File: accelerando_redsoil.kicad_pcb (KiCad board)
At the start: 2 copper layers, 24.1 x 26.7 mm, 8 parts, among them J1 Conn_01x10, J2 Conn_01x10, J3 Conn_01x05_Female, J4 Conn_01x04_Male, U1 eByte E73-2G4M08S1C-52840

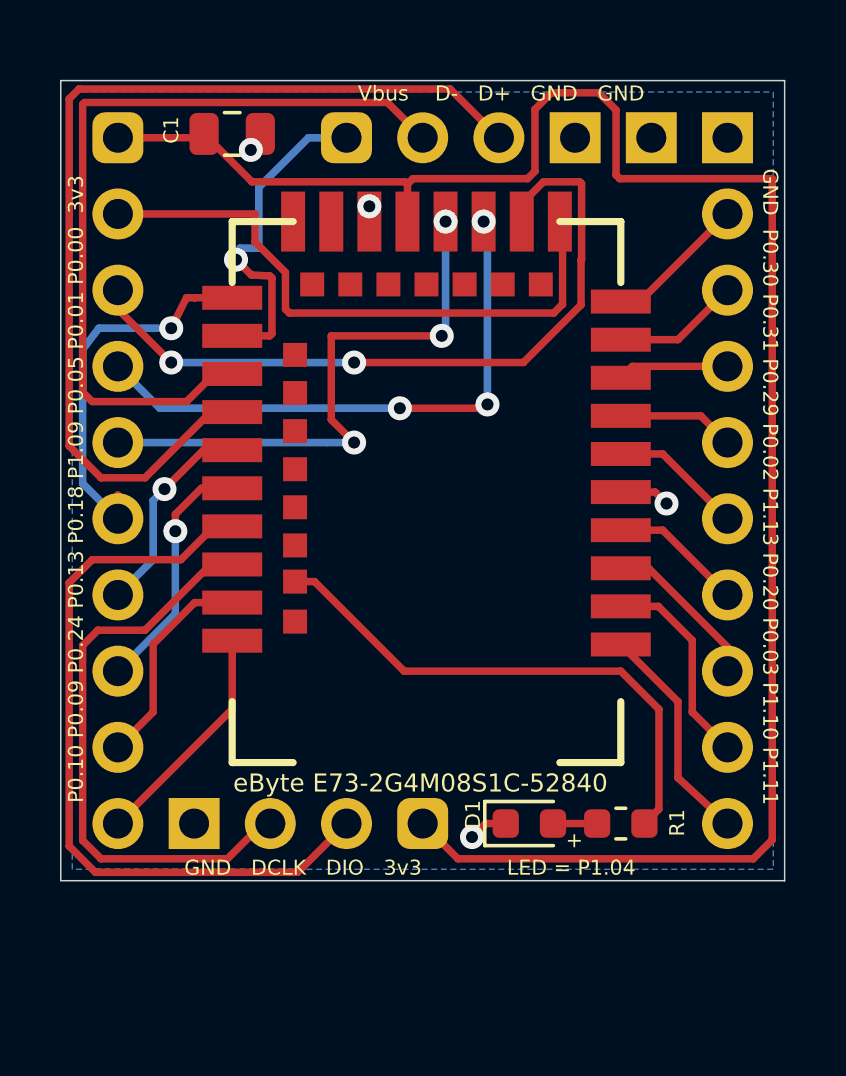
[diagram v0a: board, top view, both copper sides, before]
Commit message: Redsoil PCB 1.1 - USB power, Battery conn, JST PH SWD
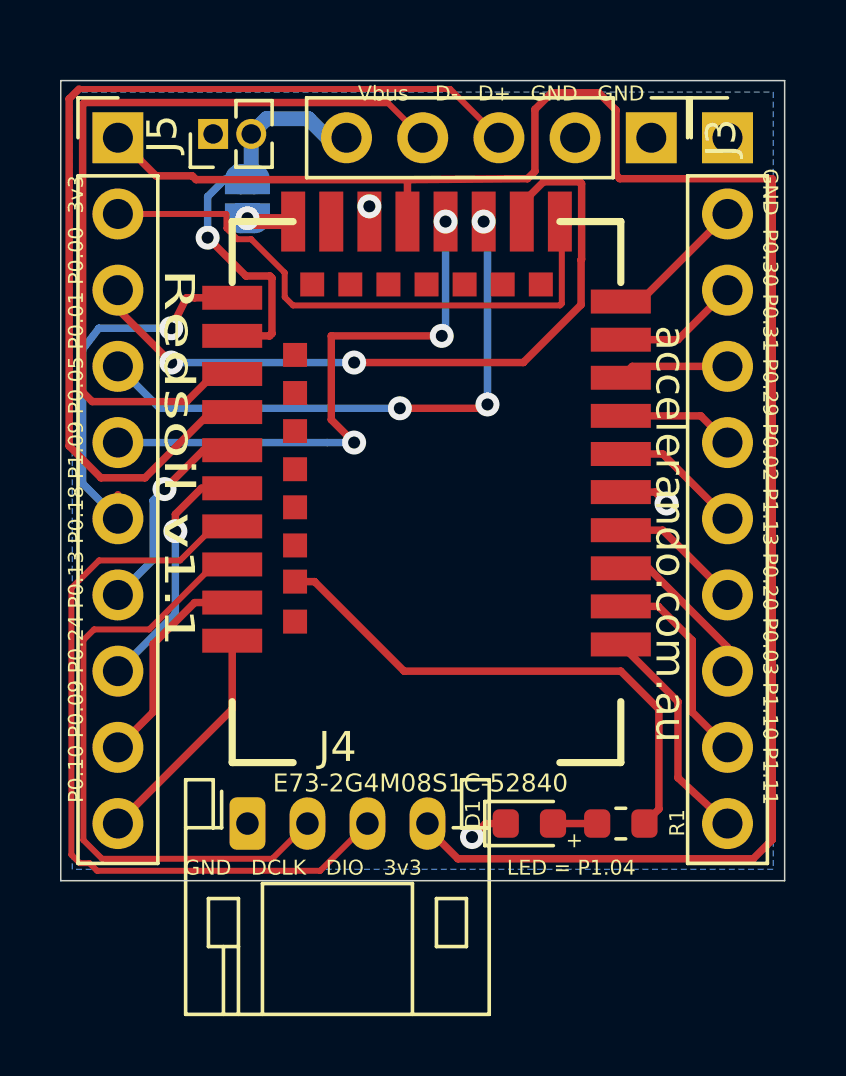
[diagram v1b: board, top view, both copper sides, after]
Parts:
- removed C1: C, Capacitor_SMD:C_0805_2012Metric
- added J5: Batt, Connector_PinHeader_1.27mm:PinHeader_1x02_P1.27mm_Vertical, F.Cu at (92.1, 58.3)
- added JP1: Jumper_2_Bridged, Jumper:SolderJumper-2_P1.3mm_Open_RoundedPad1.0x1.5mm, B.Cu at (93.2, 60.5)
- J1: value Conn_01x10 -> IOA; footprint Accelerando:PinHeader_1x10_P2.54mm_Vertical_nooutline -> Connector_PinHeader_2.54mm:PinHeader_1x10_P2.54mm_Vertical
- J2: value Conn_01x10 -> IOB; footprint Accelerando:PinHeader_1x10_P2.54mm_Vertical_nooutline -> Connector_PinHeader_2.54mm:PinHeader_1x10_P2.54mm_Vertical
- J3: value Conn_01x05_Female -> USB; footprint Accelerando:PinHeader_1x05_P2.54mm_Vertical_nooutline -> Connector_PinHeader_2.54mm:PinHeader_1x05_P2.54mm_Vertical
- J4: value Conn_01x04_Male -> SWD; footprint Connector_PinHeader_2.54mm:PinHeader_1x04_P2.54mm_Vertical -> Connector_JST:JST_PH_S4B-PH-K_1x04_P2.00mm_Horizontal
- U1: value eByte E73-2G4M08S1C-52840 -> E73-2G4M08S1C-52840
- moved J3 10.2 mm to (106.7, 58.4), turned to 270 degrees
- moved J4 1.78 mm to (93.2, 81.3), turned to 0 degrees
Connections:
- J3 pad 1: /VBUS -> /GND
- J3 pad 2: /D- -> /GND
- J3 pad 4: /GND -> /D-
- J3 pad 5: /GND -> /VBUS
- U1 pad 12: (no net) -> Net-(U1-Pad12)
- U1 pad 14: (no net) -> Net-(U1-Pad14)
- U1 pad 16: (no net) -> Net-(U1-Pad16)
- U1 pad 18: (no net) -> Net-(U1-Pad18)
- U1 pad 20: (no net) -> Net-(U1-Pad20)
- U1 pad 22: (no net) -> Net-(U1-Pad22)
- U1 pad 23: (no net) -> Net-(U1-Pad23)
- U1 pad 24: (no net) -> Net-(U1-Pad24)
- U1 pad 25: (no net) -> Net-(JP1-Pad2)
- U1 pad 28: (no net) -> Net-(U1-Pad28)
- U1 pad 30: (no net) -> Net-(U1-Pad30)
- U1 pad 32: (no net) -> Net-(U1-Pad32)
- U1 pad 34: (no net) -> Net-(U1-Pad34)
- U1 pad 36: (no net) -> Net-(U1-Pad36)
- U1 pad 38: (no net) -> Net-(U1-Pad38)
- U1 pad 42: (no net) -> Net-(U1-Pad42)
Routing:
- net /VBUS: track 11.3 -> 14.6 mm
- net /SWDCLK: track 19.6 -> 21.6 mm
- net Net-(JP1-Pad2): track 0.00 -> 1.57 mm, vias 0 -> 1
- net /GND: track 4.17 -> 3.50 mm, vias 4 -> 3
- net /P0.00: track 20.4 -> 19.7 mm
- net /SWDIO: track 25.3 -> 25.8 mm
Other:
- board text added: "Accelerando Redsoil"
- board text added: "BTN1"
- board text added: "BTN2"
- board text added: "MISO"
- board text added: "MOSI"
- board text added: "RST"
- board text added: "Redsoil v1.1"
- board text added: "Rx"
- board text added: "SCK"
- board text added: "SCL"
- board text added: "SDA"
- board text added: "Tx"
- board text added: "accelerando.com.au"
- board text added: "©2020 accelerando.com.au v1.1 2021-04–20"
- board text removed: "©2020 accelerando.com.au v1.0 2020-08–03"
